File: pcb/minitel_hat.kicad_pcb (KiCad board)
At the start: 2 copper layers, 65 x 56 mm, 0 parts

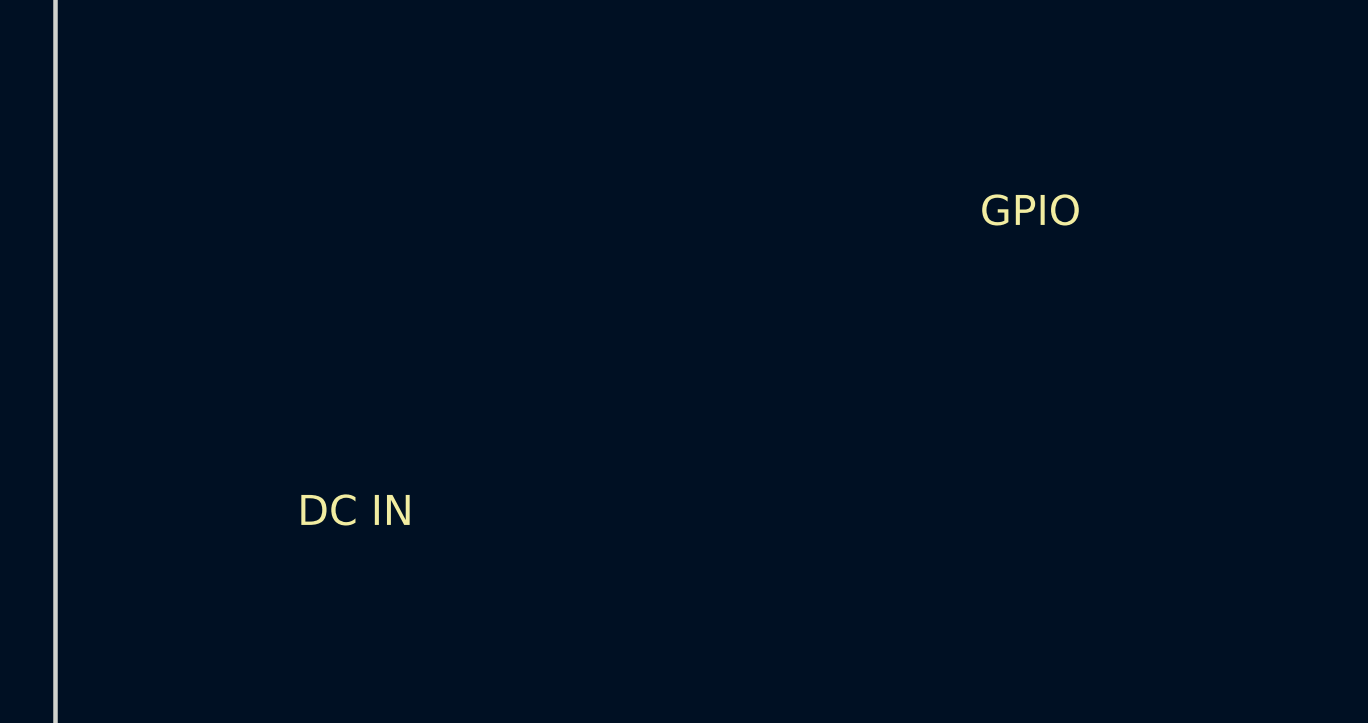
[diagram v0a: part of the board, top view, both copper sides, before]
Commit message: fix: correction syntaxe fichiers KiCad (suppression commentaires invalides)
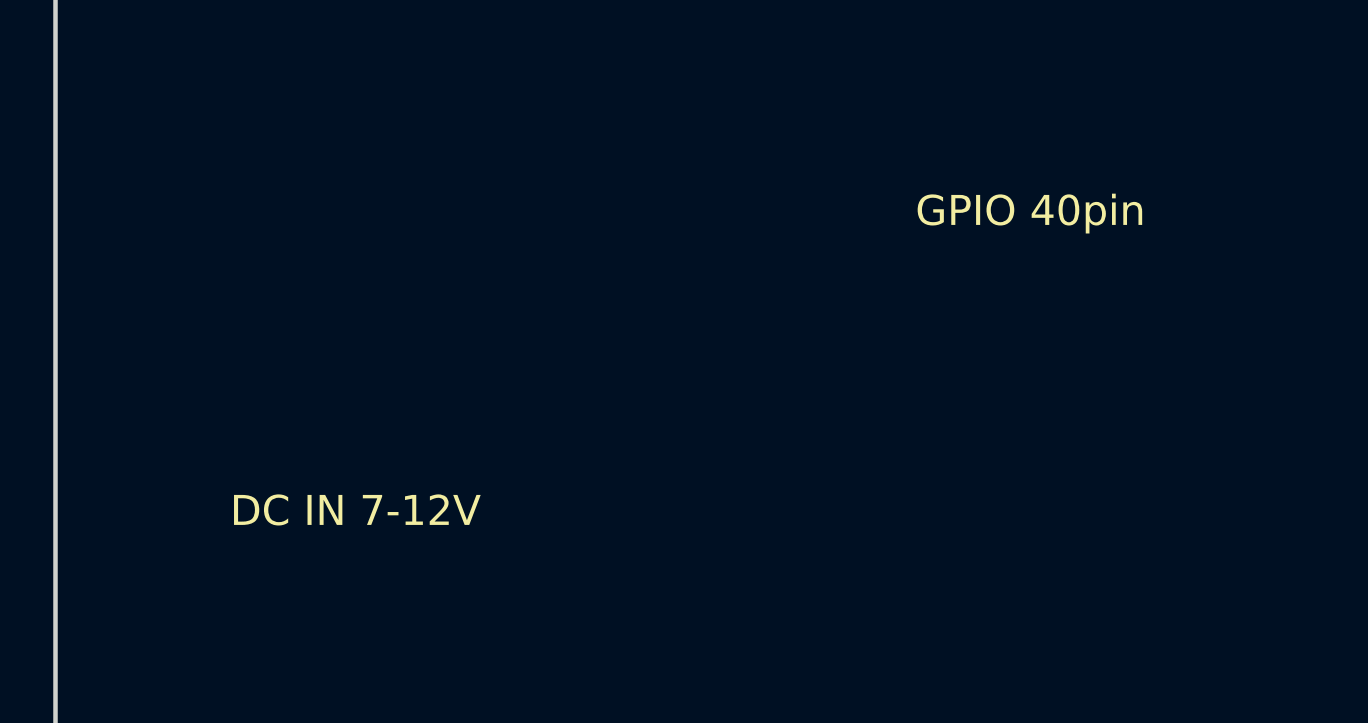
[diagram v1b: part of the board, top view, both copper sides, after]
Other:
- board text added: "DC IN 7-12V"
- board text added: "GPIO 40pin"
- board text removed: "DC IN"
- board text removed: "GPIO"
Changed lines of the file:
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@@
     (rev "1.0")
     (company "M-Kiwi Project")
-    (comment 1 "PROTOTYPE NON TESTÉ")
-    (comment 2 "Dimensions: 65mm x 56mm (format HAT standard)")
+    (comment 1 "PROTOTYPE NON TESTE")
+    (comment 2 "Dimensions: 65mm x 56mm")
   )
   (layers
@@
     (48 "B.Fab" user)
     (49 "F.Fab" user)
-    (50 "User.1" user)
-    (51 "User.2" user)
-    (52 "User.3" user)
-    (53 "User.4" user)
-    (54 "User.5" user)
-    (55 "User.6" user)
-    (56 "User.7" user)
-    (57 "User.8" user)
-    (58 "User.9" user)
   )
   (setup
@@
   (net 12 "LED1")
   (net 13 "LED2")
-  ;; Board outline - HAT Raspberry Pi standard 65x56mm
   (gr_rect
     (start 0 0)
@@
     (fill none)
     (layer "Edge.Cuts")
-    (uuid "board-outline")
-  )
-  ;; Mounting holes M2.5
+  )
   (gr_circle
     (center 3.5 3.5)
@@
     (fill none)
     (layer "Edge.Cuts")
-    (uuid "hole-1")
   )
   (gr_circle
@@
     (fill none)
     (layer "Edge.Cuts")
-    (uuid "hole-2")
   )
   (gr_circle
@@
     (fill none)
     (layer "Edge.Cuts")
-    (uuid "hole-3")
   )
   (gr_circle
@@
     (fill none)
     (layer "Edge.Cuts")
-    (uuid "hole-4")
-  )
-  ;; Title on silkscreen
+  )
   (gr_text "M-KIWI HAT v1.0"
     (at 32.5 5 0)
     (layer "F.SilkS")
-    (uuid "title-text")
     (effects
       (font (size 2 2) (thickness 0.3))
@@
     (at 32.5 51 0)
     (layer "F.SilkS")
-    (uuid "prototype-text")
     (effects
       (font (size 1.5 1.5) (thickness 0.2))
@@
     )
   )
-  ;; Component labels
-  (gr_text "GPIO"
+  (gr_text "GPIO 40pin"
     (at 32.5 15 0)
     (layer "F.SilkS")
-    (uuid "gpio-label")
     (effects
       (font (size 1 1) (thickness 0.15))
@@
     (at 10 35 0)
     (layer "F.SilkS")
-    (uuid "din-label")
     (effects
       (font (size 1 1) (thickness 0.15))
@@
     (at 55 35 0)
     (layer "F.SilkS")
-    (uuid "oled-label")
     (effects
       (font (size 1 1) (thickness 0.15))
@@
     (at 20 45 0)
     (layer "F.SilkS")
-    (uuid "btn1-label")
     (effects
       (font (size 0.8 0.8) (thickness 0.12))
@@
     (at 30 45 0)
     (layer "F.SilkS")
-    (uuid "btn2-label")
     (effects
       (font (size 0.8 0.8) (thickness 0.12))
@@
     (at 40 45 0)
     (layer "F.SilkS")
-    (uuid "btn3-label")
     (effects
       (font (size 0.8 0.8) (thickness 0.12))
@@
     (at 50 45 0)
     (layer "F.SilkS")
-    (uuid "led1-label")
     (effects
       (font (size 0.8 0.8) (thickness 0.12))
@@
     (at 57 45 0)
     (layer "F.SilkS")
-    (uuid "led2-label")
-    (effects
-      (font (size 0.8 0.8) (thickness 0.12))
-      (justify center)
-    )
-  )
-  (gr_text "DC IN"
+    (effects
+      (font (size 0.8 0.8) (thickness 0.12))
+      (justify center)
+    )
+  )
+  (gr_text "DC IN 7-12V"
     (at 10 25 0)
     (layer "F.SilkS")
-    (uuid "dcin-label")
-    (effects
-      (font (size 1 1) (thickness 0.15))
+    (effects
+      (font (size 1 1) (thickness 0.15))
